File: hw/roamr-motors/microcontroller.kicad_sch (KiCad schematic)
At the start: 22 parts, among them Q1 L8050QLT1G, Q2 QL8050QLT1G, SW1 SW_MEC_5G, SW2 SW_MEC_5G, U3 ESP32-S3-WROOM-1, U4 CP2102N-A02-GQFN28

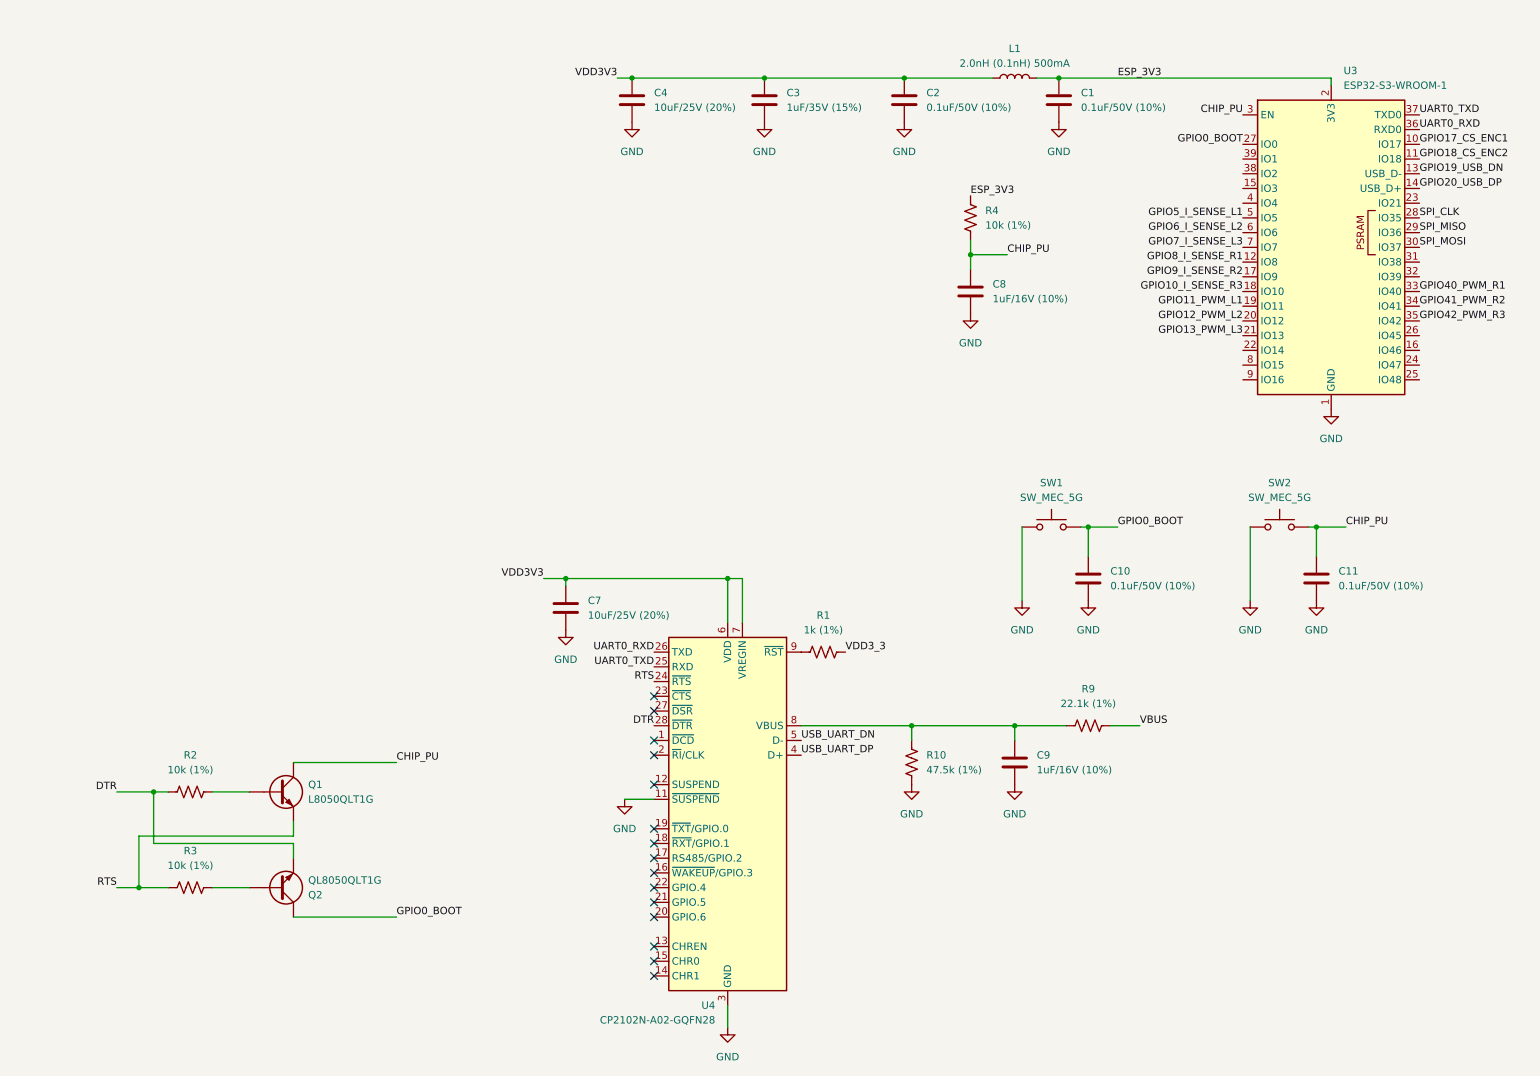
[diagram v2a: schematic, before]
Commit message: finished schematic and assigning most footprints
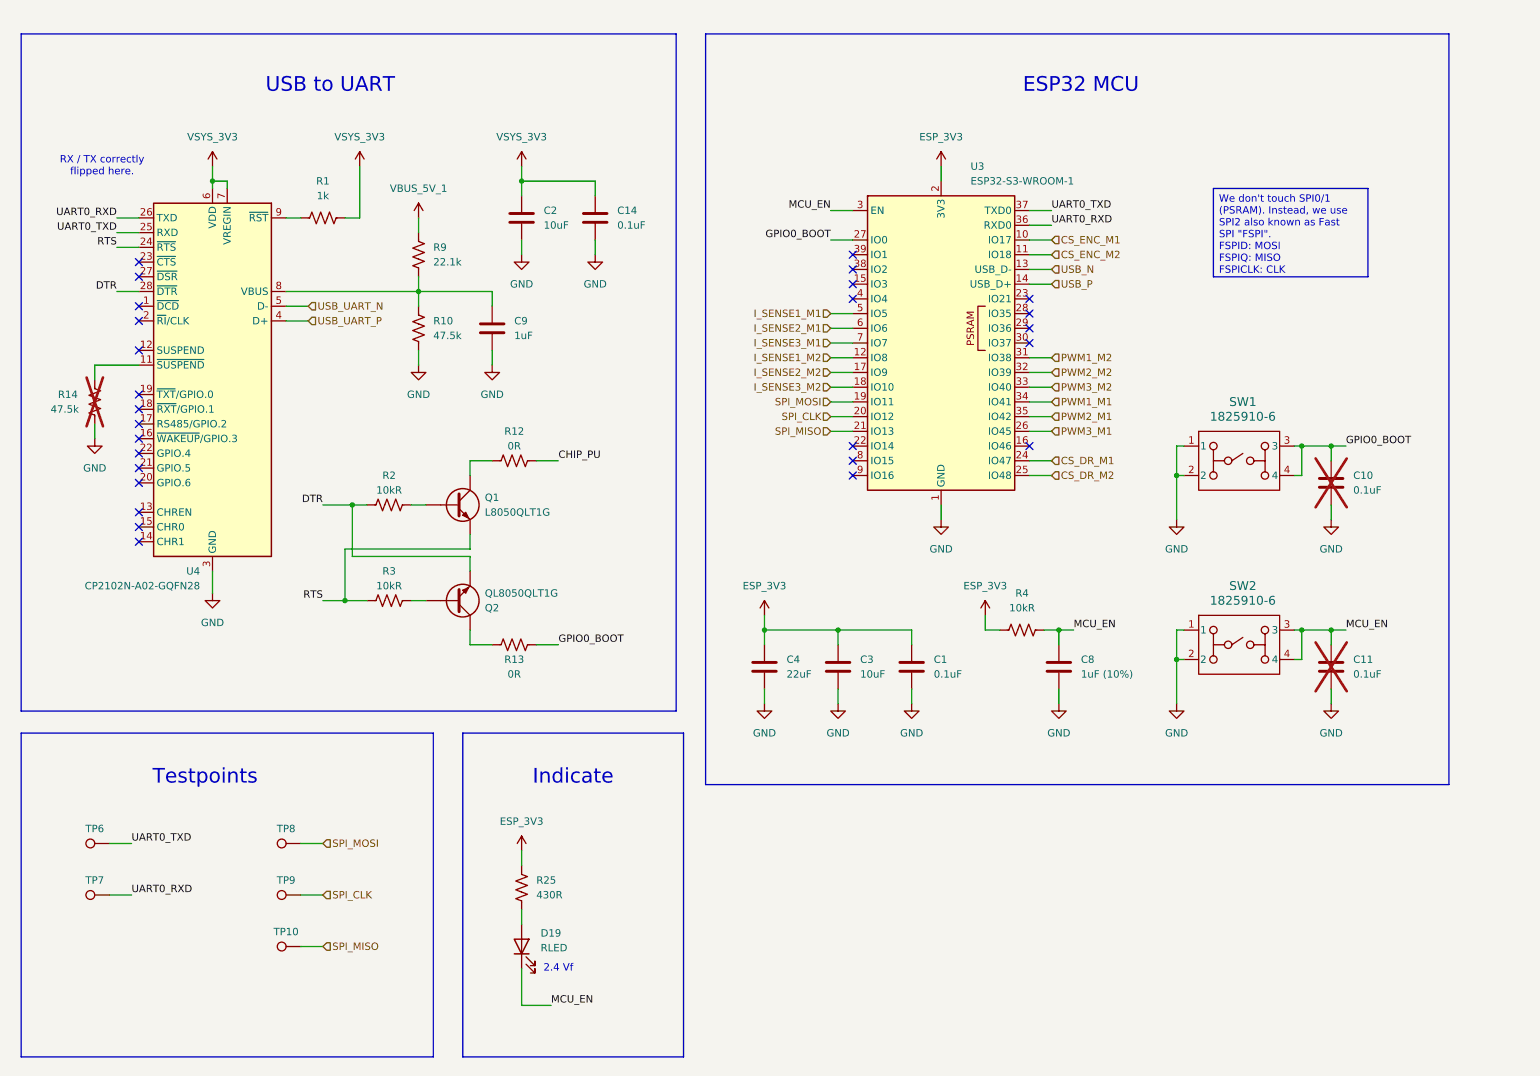
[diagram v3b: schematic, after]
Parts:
- removed C7: 10uF/25V (20%), symbol Device:C
- removed L1: 2.0nH (0.1nH) 500mA, symbol Device:L
- removed SW1, SW2: SW_MEC_5G, symbol Switch:SW_MEC_5G
- added C14: 0.1uF, Capacitor_SMD:C_0603_1608Metric, symbol Device:C
- added D19: RLED, KT-0603:LEDC1608X70N, symbol Device:LED
- added R12, R13: 0R, Resistor_SMD:R_0603_1608Metric, symbol Device:R_US
- added R14: 47.5k, Resistor_SMD:R_0603_1608Metric, symbol Device:R_US
- added R25: 430R, Resistor_SMD:R_0603_1608Metric, symbol Device:R_US
- added SW1, SW2: 1825910-6, 1825910_6:SW4_1825910-B_TEC, symbol 1825910_6:1825910-6
- added TP10, TP6, TP7, TP8, TP9: TestPoint, TestPoint:TestPoint_Pad_D1.5mm, symbol Connector:TestPoint
- C1: value 0.1uF/50V (10%) -> 0.1uF; footprint (none) -> Capacitor_SMD:C_0603_1608Metric
- C10, C11: value 0.1uF/50V (10%) -> 0.1uF; footprint (none) -> Capacitor_SMD:C_0603_1608Metric; now not fitted
- C2: value 0.1uF/50V (10%) -> 10uF; footprint (none) -> Capacitor_SMD:C_0603_1608Metric
- C3: value 1uF/35V (15%) -> 10uF; footprint (none) -> Capacitor_SMD:C_0603_1608Metric
- C4: value 10uF/25V (20%) -> 22uF; footprint (none) -> Capacitor_SMD:C_0603_1608Metric
- C8: value 1uF/16V (10%) -> 1uF (10%); footprint (none) -> Capacitor_SMD:C_0603_1608Metric
- C9: value 1uF/16V (10%) -> 1uF; footprint (none) -> Capacitor_SMD:C_0603_1608Metric
- R1: value 1k (1%) -> 1k; footprint (none) -> Resistor_SMD:R_0603_1608Metric
- R10: value 47.5k (1%) -> 47.5k; footprint (none) -> Resistor_SMD:R_0603_1608Metric
- R2, R3, R4: value 10k (1%) -> 10kR; footprint (none) -> Resistor_SMD:R_0603_1608Metric
- R9: value 22.1k (1%) -> 22.1k; footprint (none) -> Resistor_SMD:R_0603_1608Metric
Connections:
- net GPIO11_PWM_L1 is gone; now on net SPI_MOSI: U3.19 (IO11)
- net GPIO12_PWM_L2 is gone; now on net SPI_CLK: U3.20 (IO12)
- net GPIO13_PWM_L3 is gone; now on net SPI_MISO: U3.21 (IO13)
- net VDD3_3 is gone; now on net VSYS_3V3: R1.2
- net CHIP_PU: now also R12.2; no longer C11.1, C8.1, Q1.C, R4.2, U3.3 (EN)
- net ESP_3V3: now also C3.1, C4.1, R25.2
- net GND: now also C14.2, R14.1, SW1.1, SW1.2, SW2.1, SW2.2; no longer U4.11 (~{SUSPEND})
- net GPIO0_BOOT: now also R13.2, SW1.3, SW1.4; no longer Q2.C
- net SPI_CLK: now also TP9.1; no longer U3.28 (IO35)
- net SPI_MISO: now also TP10.1; no longer U3.29 (IO36)
- net SPI_MOSI: now also TP8.1; no longer U3.30 (IO37)
- net UART0_RXD: now also TP7.1
- net UART0_TXD: now also TP6.1
- net CS_DR_M1: now reaches U3.24 (IO47)
- net CS_DR_M2: now reaches U3.25 (IO48)
- net PWM3_M1: now reaches U3.26 (IO45)
- net PWM1_M2: now reaches U3.31 (IO38)
- net PWM2_M2: now reaches U3.32 (IO39)
- net GPIO10_I_SENSE_R3 renamed I_SENSE3_M2
- net GPIO17_CS_ENC1 renamed CS_ENC_M1
- net GPIO18_CS_ENC2 renamed CS_ENC_M2
- net GPIO19_USB_DN renamed USB_N
- net GPIO20_USB_DP renamed USB_P
- net GPIO40_PWM_R1 renamed PWM3_M2
- net GPIO41_PWM_R2 renamed PWM1_M1
- net GPIO42_PWM_R3 renamed PWM2_M1
- net GPIO5_I_SENSE_L1 renamed I_SENSE1_M1
- net GPIO6_I_SENSE_L2 renamed I_SENSE2_M1
- net GPIO7_I_SENSE_L3 renamed I_SENSE3_M1
- net GPIO8_I_SENSE_R1 renamed I_SENSE1_M2
- net GPIO9_I_SENSE_R2 renamed I_SENSE2_M2
- net USB_UART_DN renamed USB_UART_N
- net USB_UART_DP renamed USB_UART_P
- net VBUS renamed VBUS_5V_1
- net VDD3V3 renamed VSYS_3V3
- net VSYS_3V3: now also C14.1; no longer C3.1, C4.1
- new net: Q2.C, R13.1
- new net: Q1.C, R12.1
- new net: R14.2, U4.11 (~{SUSPEND})
- new net: D19.2 (A), R25.1
- new net MCU_EN: C11.1, C8.1, D19.1 (K), R4.2, SW2.3, SW2.4, U3.3 (EN)
- no-connect marks 15 -> 27
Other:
- note added: "2.4 Vf"
- note added: "ESP32 MCU"
- note added: "Indicate"
- note added: "RX / TX correctly flipped here."
- note added: "Testpoints"
- note added: "USB to UART"
- company: (none) -> Mechatronics FYDP Group 16
- moved on the sheet: C1, C3, C4, C8, C9, Q1, Q2, R1, R10, R2, R3, R4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

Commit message: added all footprints, starting layout properly
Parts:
- C8: value 1uF (10%) -> 1uF
- Q1: footprint (none) -> L8050QLT1G:L8050QLT1G
- Q2: value QL8050QLT1G -> L8050QLT1G; footprint (none) -> L8050QLT1G:L8050QLT1G
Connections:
- net CHIP_PU is gone; now on net MCU_EN: R12.2
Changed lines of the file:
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@@
 		)
 	)
-	(label "CHIP_PU"
+	(label "MCU_EN"
 		(at 109.22 92.71 0)
 		(effects
@@
 	)
 	(symbol
-		(lib_id "Device:Q_NPN")
-		(at 91.44 116.84 0)
-		(mirror x)
-		(unit 1)
-		(exclude_from_sim no)
-		(in_bom yes)
-		(on_board yes)
-		(dnp no)
-		(property "Reference" "Q2"
-			(at 96.52 118.11 0)
-			(effects
-				(font
-					(size 1.27 1.27)
-				)
-				(justify left)
-			)
-		)
-		(property "Value" "QL8050QLT1G"
-			(at 96.52 115.57 0)
-			(effects
-				(font
-					(size 1.27 1.27)
-				)
-				(justify left)
-			)
-		)
-		(property "Footprint" ""
-			(at 96.52 119.38 0)
-			(effects
-				(font
-					(size 1.27 1.27)
-				)
-				(hide yes)
-			)
-		)
-		(property "Datasheet" "~"
-			(at 91.44 116.84 0)
-			(effects
-				(font
-					(size 1.27 1.27)
-				)
-				(hide yes)
-			)
-		)
-		(property "Description" "NPN bipolar junction transistor"
-			(at 91.44 116.84 0)
-			(effects
-				(font
-					(size 1.27 1.27)
-				)
-				(hide yes)
-			)
-		)
-		(pin "E"
-		)
-		(pin "C"
-		)
-		(pin "B"
-		)
-		(instances
-			(project "roamr-motors"
-				(path "/db664d1d-d972-4e66-af85-94b6971e1c6e/206ea9a6-1e38-4e76-a070-d60887d5750e"
-					(reference "Q2")
-					(unit 1)
-				)
-			)
-		)
-	)
-	(symbol
 		(lib_id "Device:C")
 		(at 115.57 50.8 0)
@@
 			)
 		)
-		(property "Footprint" ""
+		(property "Footprint" "L8050QLT1G:L8050QLT1G"
 			(at 96.52 97.79 0)
 			(effects
@@
 	)
 	(symbol
+		(lib_id "Device:Q_NPN")
+		(at 91.44 116.84 0)
+		(mirror x)
+		(unit 1)
+		(exclude_from_sim no)
+		(in_bom yes)
+		(on_board yes)
+		(dnp no)
+		(property "Reference" "Q2"
+			(at 96.52 118.1101 0)
+			(effects
+				(font
+					(size 1.27 1.27)
+				)
+				(justify left)
+			)
+		)
+		(property "Value" "L8050QLT1G"
+			(at 96.52 115.5701 0)
+			(effects
+				(font
+					(size 1.27 1.27)
+				)
+				(justify left)
+			)
+		)
+		(property "Footprint" "L8050QLT1G:L8050QLT1G"
+			(at 96.52 119.38 0)
+			(effects
+				(font
+					(size 1.27 1.27)
+				)
+				(hide yes)
+			)
+		)
+		(property "Datasheet" "~"
+			(at 91.44 116.84 0)
+			(effects
+				(font
+					(size 1.27 1.27)
+				)
+				(hide yes)
+			)
+		)
+		(property "Description" "NPN bipolar junction transistor"
+			(at 91.44 116.84 0)
+			(effects
+				(font
+					(size 1.27 1.27)
+				)
+				(hide yes)
+			)
+		)
+		(pin "E"
+		)
+		(pin "C"
+		)
+		(pin "B"
+		)
+		(instances
+			(project "roamr-motors"
+				(path "/db664d1d-d972-4e66-af85-94b6971e1c6e/206ea9a6-1e38-4e76-a070-d60887d5750e"
+					(reference "Q2")
+					(unit 1)
+				)
+			)
+		)
+	)
+	(symbol
 		(lib_id "Device:R_US")
 		(at 68.58 50.8 90)
@@
 			)
 		)
-		(property "Value" "1uF (10%)"
+		(property "Value" "1uF"
 			(at 199.39 129.5399 0)
 			(effects

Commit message: some more layout
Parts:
- removed Q1, Q2: L8050QLT1G, L8050QLT1G:L8050QLT1G, symbol Device:Q_NPN
- added Q1, Q2: L8050QLT1G, L8050QLT1G:L8050QLT1G, symbol L8050QLT1G:L8050QLT1G
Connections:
- net DTR: now also Q2.2 (E)
- net RTS: now also Q1.2 (E)
- net at R2.2: now also Q1.1 (B)
- net at R12.1: now also Q1.3 (C)
- net at R3.2: now also Q2.1 (B)
- net at R13.1: now also Q2.3 (C)
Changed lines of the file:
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@@
-	)
-	(symbol
-		(lib_id "Device:Q_NPN")
-		(at 91.44 100.33 0)
-		(unit 1)
-		(exclude_from_sim no)
-		(in_bom yes)
-		(on_board yes)
-		(dnp no)
-		(fields_autoplaced yes)
-		(property "Reference" "Q1"
-			(at 96.52 99.0599 0)
-			(effects
-				(font
-					(size 1.27 1.27)
-				)
-				(justify left)
-			)
-		)
-		(property "Value" "L8050QLT1G"
-			(at 96.52 101.5999 0)
-			(effects
-				(font
-					(size 1.27 1.27)
-				)
-				(justify left)
-			)
-		)
-		(property "Footprint" "L8050QLT1G:L8050QLT1G"
-			(at 96.52 97.79 0)
-			(effects
-				(font
-					(size 1.27 1.27)
-				)
-				(hide yes)
-			)
-		)
-		(property "Datasheet" "~"
-			(at 91.44 100.33 0)
-			(effects
-				(font
-					(size 1.27 1.27)
-				)
-				(hide yes)
-			)
-		)
-		(property "Description" "NPN bipolar junction transistor"
-			(at 91.44 100.33 0)
-			(effects
-				(font
-					(size 1.27 1.27)
-				)
-				(hide yes)
-			)
-		)
-		(pin "E"
-		)
-		(pin "C"
-		)
-		(pin "B"
-		)
-		(instances
-			(project ""
-				(path "/db664d1d-d972-4e66-af85-94b6971e1c6e/206ea9a6-1e38-4e76-a070-d60887d5750e"
-					(reference "Q1")
-					(unit 1)
-				)
-			)
-		)
 	)
 	(symbol
@@
 	)
 	(symbol
-		(lib_id "Device:Q_NPN")
-		(at 91.44 116.84 0)
-		(mirror x)
-		(unit 1)
-		(exclude_from_sim no)
-		(in_bom yes)
-		(on_board yes)
-		(dnp no)
-		(property "Reference" "Q2"
-			(at 96.52 118.1101 0)
-			(effects
-				(font
-					(size 1.27 1.27)
-				)
-				(justify left)
-			)
-		)
-		(property "Value" "L8050QLT1G"
-			(at 96.52 115.5701 0)
-			(effects
-				(font
-					(size 1.27 1.27)
-				)
-				(justify left)
-			)
-		)
-		(property "Footprint" "L8050QLT1G:L8050QLT1G"
-			(at 96.52 119.38 0)
-			(effects
-				(font
-					(size 1.27 1.27)
-				)
-				(hide yes)
-			)
-		)
-		(property "Datasheet" "~"
-			(at 91.44 116.84 0)
-			(effects
-				(font
-					(size 1.27 1.27)
-				)
-				(hide yes)
-			)
-		)
-		(property "Description" "NPN bipolar junction transistor"
-			(at 91.44 116.84 0)
-			(effects
-				(font
-					(size 1.27 1.27)
-				)
-				(hide yes)
-			)
-		)
-		(pin "E"
-		)
-		(pin "C"
-		)
-		(pin "B"
-		)
-		(instances
-			(project "roamr-motors"
-				(path "/db664d1d-d972-4e66-af85-94b6971e1c6e/206ea9a6-1e38-4e76-a070-d60887d5750e"
-					(reference "Q2")
-					(unit 1)
-				)
-			)
-		)
-	)
-	(symbol
 		(lib_id "Device:R_US")
 		(at 68.58 50.8 90)
@@
 					(unit 1)
 				)
+			)
+		)
+	)
+	(symbol
+		(lib_id "L8050QLT1G:L8050QLT1G")
+		(at 86.36 100.33 0)
+		(unit 1)
+		(exclude_from_sim no)
+		(in_bom yes)
+		(on_board yes)
+		(dnp no)
+		(property "Reference" "Q1"
+			(at 98.3094 101.6184 0)
+			(effects
+				(font
+					(size 1.27 1.27)
+				)
+			)
+		)
+		(property "Value" "L8050QLT1G"
+			(at 102.87 99.06 0)
+			(effects
+				(font
+					(size 1.27 1.27)
+				)
+			)
+		)
+		(property "Footprint" "L8050QLT1G:L8050QLT1G"
+			(at 102.87 195.25 0)
+			(effects
+				(font
+					(size 1.27 1.27)
+				)
+				(justify left top)
+				(hide yes)
+			)
+		)
+		(property "Datasheet" "https://datasheet.datasheetarchive.com/originals/distributors/Datasheets-28/DSA-558356.pdf"
+			(at 102.87 295.25 0)
+			(effects
+				(font
+					(size 1.27 1.27)
+				)
+				(justify left top)
+				(hide yes)
+			)
+		)
+		(property "Description" "Trans GP BJT NPN 25V 0.8A 3-Pin SOT-23 T/R"
+			(at 86.36 100.33 0)
+			(effects
+				(font
+					(size 1.27 1.27)
+				)
+				(hide yes)
+			)
+		)
+		(property "Height" "1.11"
+			(at 102.87 495.25 0)
+			(effects
+				(font
+					(size 1.27 1.27)
+				)
+				(justify left top)
+				(hide yes)
+			)
+		)
+		(property "Manufacturer_Name" "LRC"
+			(at 102.87 595.25 0)
+			(effects
+				(font
+					(size 1.27 1.27)
+				)
+				(justify left top)
+				(hide yes)
+			)
+		)
+		(property "Manufacturer_Part_Number" "L8050QLT1G"
+			(at 102.87 695.25 0)
+			(effects
+				(font
+					(size 1.27 1.27)
+				)
+				(justify left top)
+				(hide yes)
+			)
+		)
+		(property "Mouser Part Number" ""
+			(at 102.87 795.25 0)
+			(effects
+				(font
+					(size 1.27 1.27)
+				)
+				(justify left top)
+				(hide yes)
+			)
+		)
+		(property "Mouser Price/Stock" ""
+			(at 102.87 895.25 0)
+			(effects
+				(font
+					(size 1.27 1.27)
+				)
+				(justify left top)
+				(hide yes)
+			)
+		)
+		(property "Arrow Part Number" ""
+			(at 102.87 995.25 0)
+			(effects
+				(font
+					(size 1.27 1.27)
+				)
+				(justify left top)
+				(hide yes)
+			)
+		)
+		(property "Arrow Price/Stock" ""
+			(at 102.87 1095.25 0)
+			(effects
+				(font
+					(size 1.27 1.27)
+				)
+				(justify left top)
+				(hide yes)
+			)
+		)
+		(pin "3"
+		)
+		(pin "2"
+		)
+		(pin "1"
+		)
+		(instances
+			(project "roamr-motors"
+				(path "/db664d1d-d972-4e66-af85-94b6971e1c6e/206ea9a6-1e38-4e76-a070-d60887d5750e"
+					(reference "Q1")
+					(unit 1)
+				)
+			)
+		)
+	)
+	(symbol
+		(lib_id "L8050QLT1G:L8050QLT1G")
+		(at 86.36 116.84 0)
+		(mirror x)
+		(unit 1)
+		(exclude_from_sim no)
+		(in_bom yes)
+		(on_board yes)
+		(dnp no)
+		(property "Reference" "Q2"
+			(at 98.3094 115.5516 0)
+			(effects
+				(font
+					(size 1.27 1.27)
+				)
+			)
+		)
+		(property "Value" "L8050QLT1G"
+			(at 102.87 118.11 0)
+			(effects
+				(font
+					(size 1.27 1.27)
+				)
+			)
+		)
+		(property "Footprint" "L8050QLT1G:L8050QLT1G"
+			(at 102.87 21.92 0)
+			(effects
+				(font
+					(size 1.27 1.27)
+				)
+				(justify left top)
+				(hide yes)
+			)
+		)
+		(property "Datasheet" "https://datasheet.datasheetarchive.com/originals/distributors/Datasheets-28/DSA-558356.pdf"
+			(at 102.87 -78.08 0)
+			(effects
+				(font
+					(size 1.27 1.27)
+				)
+				(justify left top)
+				(hide yes)
+			)
+		)
+		(property "Description" "Trans GP BJT NPN 25V 0.8A 3-Pin SOT-23 T/R"
+			(at 86.36 116.84 0)
+			(effects
+				(font
+					(size 1.27 1.27)
+				)
+				(hide yes)
+			)
+		)
+		(property "Height" "1.11"
+			(at 102.87 -278.08 0)
+			(effects
+				(font
+					(size 1.27 1.27)
+				)
+				(justify left top)
+				(hide yes)
+			)
+		)
+		(property "Manufacturer_Name" "LRC"
+			(at 102.87 -378.08 0)
+			(effects
+				(font
+					(size 1.27 1.27)
+				)
+				(justify left top)
+				(hide yes)
+			)
+		)
+		(property "Manufacturer_Part_Number" "L8050QLT1G"
+			(at 102.87 -478.08 0)
+			(effects
+				(font
+					(size 1.27 1.27)
+				)
+				(justify left top)
+				(hide yes)
+			)
+		)
+		(property "Mouser Part Number" ""
+			(at 102.87 -578.08 0)
+			(effects
+				(font
+					(size 1.27 1.27)
+				)
+				(justify left top)
+				(hide yes)
+			)
+		)
+		(property "Mouser Price/Stock" ""
+			(at 102.87 -678.08 0)
+			(effects
+				(font
+					(size 1.27 1.27)
+				)
+				(justify left top)
+				(hide yes)
+			)
+		)
+		(property "Arrow Part Number" ""
+			(at 102.87 -778.08 0)
+			(effects
+				(font
+					(size 1.27 1.27)
+				)
+				(justify left top)
+				(hide yes)
+			)
+		)
+		(property "Arrow Price/Stock" ""
+			(at 102.87 -878.08 0)
+			(effects
+				(font
+					(size 1.27 1.27)
+				)
+				(justify left top)
+				(hide yes)
+			)
+		)
+		(pin "3"
+		)
+		(pin "2"
+		)
+		(pin "1"
+		)
+		(instances
+			(project ""
+				(path "/db664d1d-d972-4e66-af85-94b6971e1c6e/206ea9a6-1e38-4e76-a070-d60887d5750e"
+					(reference "Q2")
+					(unit 1)
+				)

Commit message: more layout, i think i get do it on one side
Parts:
- removed C9: 1uF, Capacitor_SMD:C_0603_1608Metric, symbol Device:C
- C5: renamed from C2; value 10uF -> 4.7uF
- renumbered C8 to C10, C10 to C11, C11 to C12, C14 to C6, C4 to C7, C3 to C8, C1 to C9, R14 to R10, R1 to R11, R2 to R12, R3 to R13, R9 to R14, R10 to R15, R12 to R16, R13 to R17, R25 to R18, R4 to R19, U4 to U2

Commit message: outputs and last minute updates
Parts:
- D19: Manufacturer_Part_Number (none) -> KT-0603R
- SW1, SW2: Manufacturer_Part_Number (none) -> 1825910-6
- U2: Manufacturer_Part_Number (none) -> CP2102N-A02-GQFN28
- U3: Manufacturer_Part_Number (none) -> ESP32-S3-WROOM-1
